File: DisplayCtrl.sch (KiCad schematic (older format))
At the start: 7 parts, among them U401 PT6315

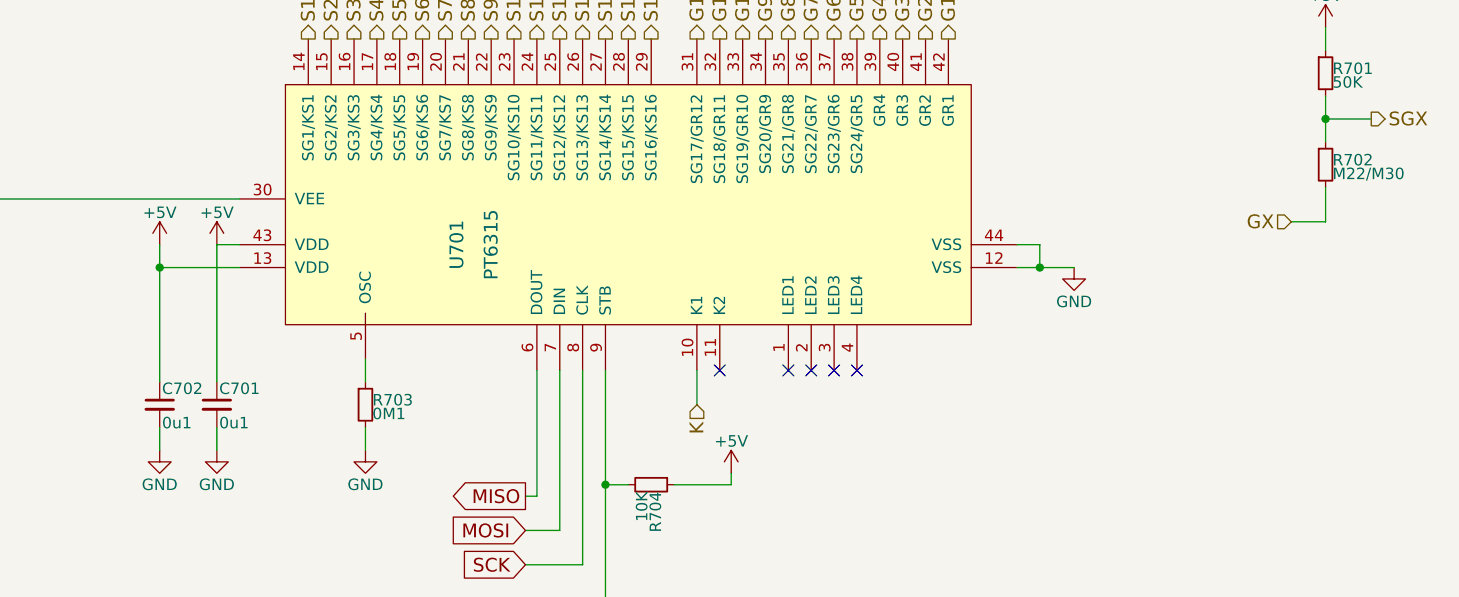
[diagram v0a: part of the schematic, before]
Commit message: switching to more convenient notation of values, e.g. 100K instead of 0M1
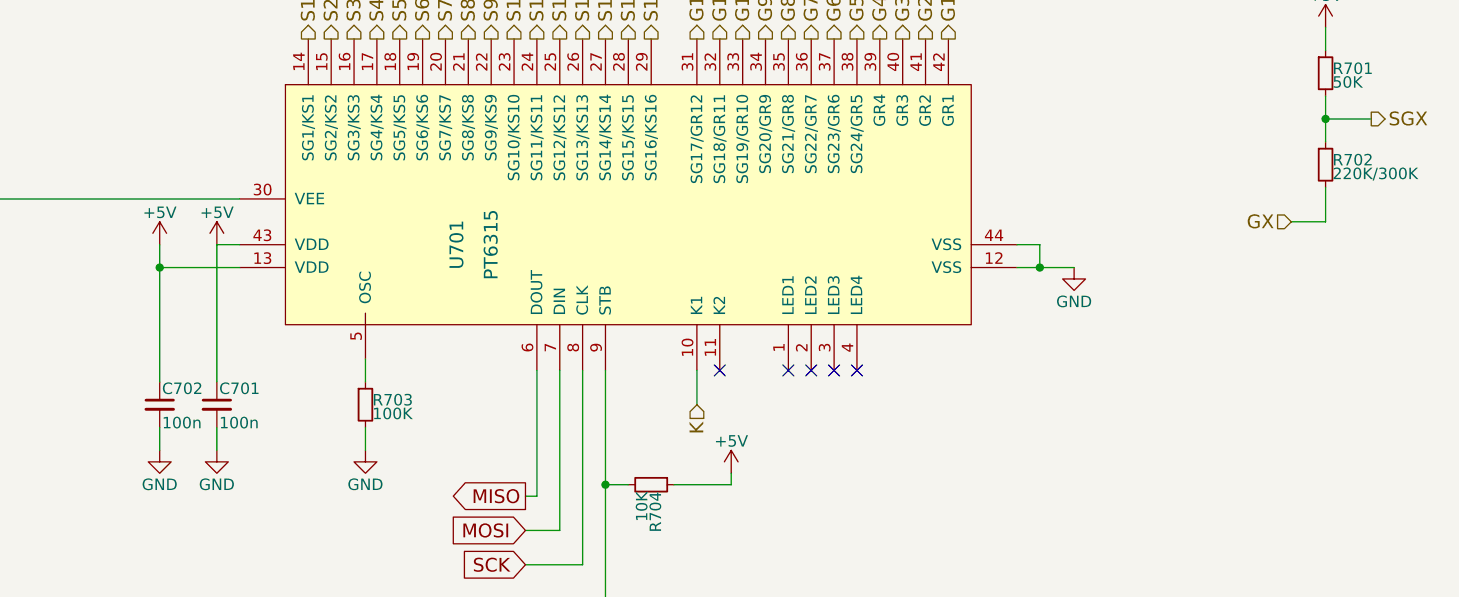
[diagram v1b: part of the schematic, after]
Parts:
- C401, C402: value 0u1 -> 100n
- R402: value M22/M30 -> 220K/300K
- R403: value 0M1 -> 100K
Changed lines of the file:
@@
 AR Path="/5AAC050F/5AAC05F0/5AAC0EB7" Ref="R703"  Part="1"
 F 0 "R703" H 5480 5770 50  0000 L CNN
-F 1 "0M1" H 5480 5710 50  0000 L CNN
+F 1 "100K" H 5480 5710 50  0000 L CNN
 F 2 "Resistors_SMD:R_0805_HandSoldering" H 5450 5750 50  0001 C CNN
 F 3 "" H 5450 5750 50  0001 C CNN
@@
 AR Path="/5AAC050F/5AAC05F0/5AAC8ED6" Ref="R702"  Part="1"
 F 0 "R702" H 9680 4720 50  0000 L CNN
-F 1 "M22/M30" H 9680 4660 50  0000 L CNN
+F 1 "220K/300K" H 9680 4660 50  0000 L CNN
 F 2 "Resistors_SMD:R_0805_HandSoldering" H 9650 4700 50  0001 C CNN
 F 3 "" H 9650 4700 50  0001 C CNN
@@
 AR Path="/5AAC050F/5AAC05F0/5AADCA8F" Ref="C701"  Part="1"
 F 0 "C701" H 4810 5820 50  0000 L CNN
-F 1 "0u1" H 4810 5670 50  0000 L CNN
+F 1 "100n" H 4810 5670 50  0000 L CNN
 F 2 "Capacitors_SMD:C_0805_HandSoldering" H 4800 5750 50  0001 C CNN
 F 3 "" H 4800 5750 50  0001 C CNN
@@
 AR Path="/5AAC050F/5AAC05F0/5ABABE8A" Ref="C702"  Part="1"
 F 0 "C702" H 4560 5820 50  0000 L CNN
-F 1 "0u1" H 4560 5670 50  0000 L CNN
+F 1 "100n" H 4560 5670 50  0000 L CNN
 F 2 "Capacitors_SMD:C_0805_HandSoldering" H 4550 5750 50  0001 C CNN
 F 3 "" H 4550 5750 50  0001 C CNN
